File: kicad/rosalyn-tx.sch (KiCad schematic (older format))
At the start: 38 parts, among them J1 USB-C, J2 SWD, J3 TURNIGY 9X, J4 Serial1, J5 Serial2, U1 SPX3819, U2 XC6206, U3 STM32F072C8, U4 E22-EBYTE, U5 SRV05-4

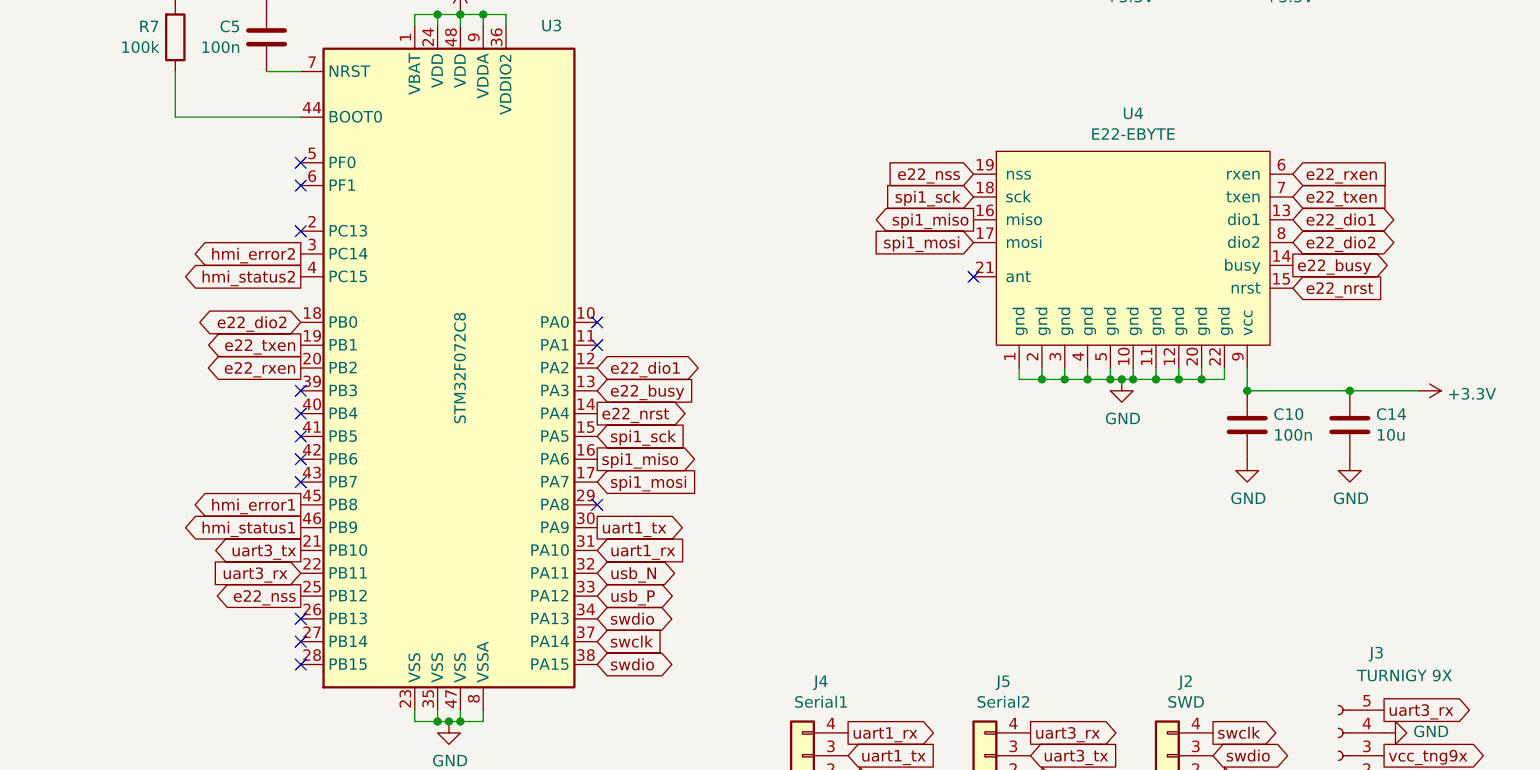
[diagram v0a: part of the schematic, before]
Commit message: added schematic with new radio port names
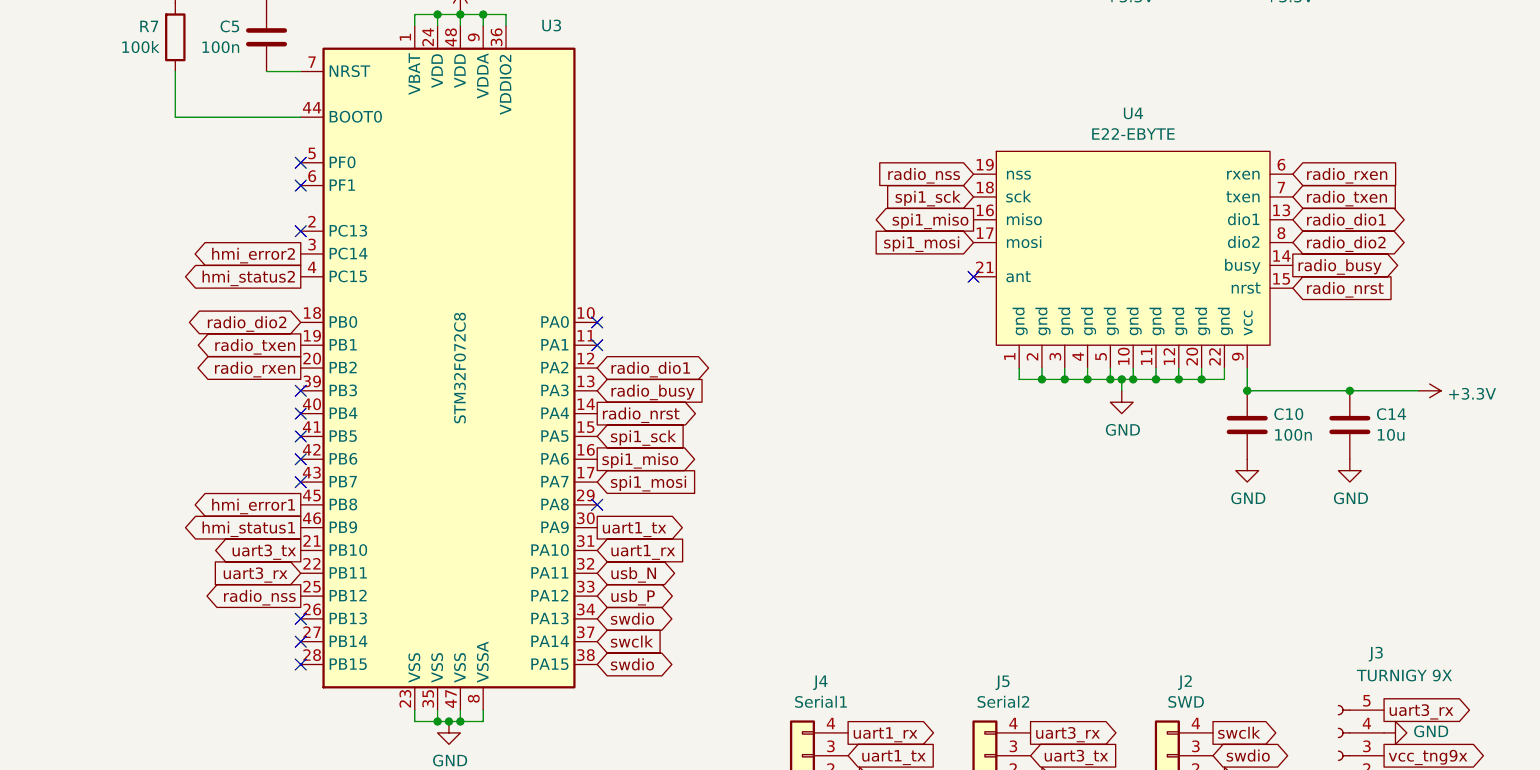
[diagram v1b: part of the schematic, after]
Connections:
- net e22_busy renamed radio_busy
- net e22_dio1 renamed radio_dio1
- net e22_dio2 renamed radio_dio2
- net e22_nrst renamed radio_nrst
- net e22_nss renamed radio_nss
- net e22_rxen renamed radio_rxen
- net e22_txen renamed radio_txen
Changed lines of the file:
@@
 L power:GND #PWR037
 U 1 1 5FC6AB21
-P 9050 3900
+P 9050 3950
 AR Path="/5FC6AB21" Ref="#PWR037"  Part="1"
 AR Path="/5FC29817/5FC6AB21" Ref="#PWR?"  Part="1"
-F 0 "#PWR037" H 9050 3650 50  0001 C CNN
-F 1 "GND" H 9055 3727 50  0000 C CNN
-F 2 "" H 9050 3900 50  0001 C CNN
-F 3 "" H 9050 3900 50  0001 C CNN
-	1    9050 3900
+F 0 "#PWR037" H 9050 3700 50  0001 C CNN
+F 1 "GND" H 9055 3777 50  0000 C CNN
+F 2 "" H 9050 3950 50  0001 C CNN
+F 3 "" H 9050 3950 50  0001 C CNN
+	1    9050 3950
 	1    0    0    -1
 $EndComp
@@
 $EndComp
 Text GLabel 9800 3000 2    50   Input ~ 0
-e22_rxen
+radio_rxen
 Text GLabel 9800 3100 2    50   Input ~ 0
-e22_txen
+radio_txen
 Text GLabel 9800 3200 2    50   BiDi ~ 0
-e22_dio1
+radio_dio1
 Text GLabel 9800 3300 2    50   BiDi ~ 0
-e22_dio2
+radio_dio2
 Text GLabel 9800 3400 2    50   Output ~ 0
-e22_busy
+radio_busy
 Text GLabel 9800 3500 2    50   Input ~ 0
-e22_nrst
+radio_nrst
 Text GLabel 8400 3000 0    50   Input ~ 0
-e22_nss
+radio_nss
 Text GLabel 8400 3100 0    50   Input ~ 0
 spi1_sck
@@
 usb_N
 Text GLabel 5450 3850 0    50   Output ~ 0
-e22_rxen
+radio_rxen
 Text GLabel 5450 3750 0    50   Output ~ 0
-e22_txen
+radio_txen
 Text GLabel 6750 3850 2    50   BiDi ~ 0
-e22_dio1
+radio_dio1
 Text GLabel 5450 3650 0    50   BiDi ~ 0
-e22_dio2
+radio_dio2
 Text GLabel 6750 3950 2    50   Input ~ 0
-e22_busy
+radio_busy
 Text GLabel 6750 4050 2    50   Output ~ 0
-e22_nrst
+radio_nrst
 Text GLabel 5450 4850 0    50   Output ~ 0
-e22_nss
+radio_nss
 Text GLabel 6750 4150 2    50   Input ~ 0
 spi1_sck
@@
 	0    -1   -1   0
 $EndComp
+Wire Wire Line
+	9050 3950 9050 3900
 $EndSCHEMATC

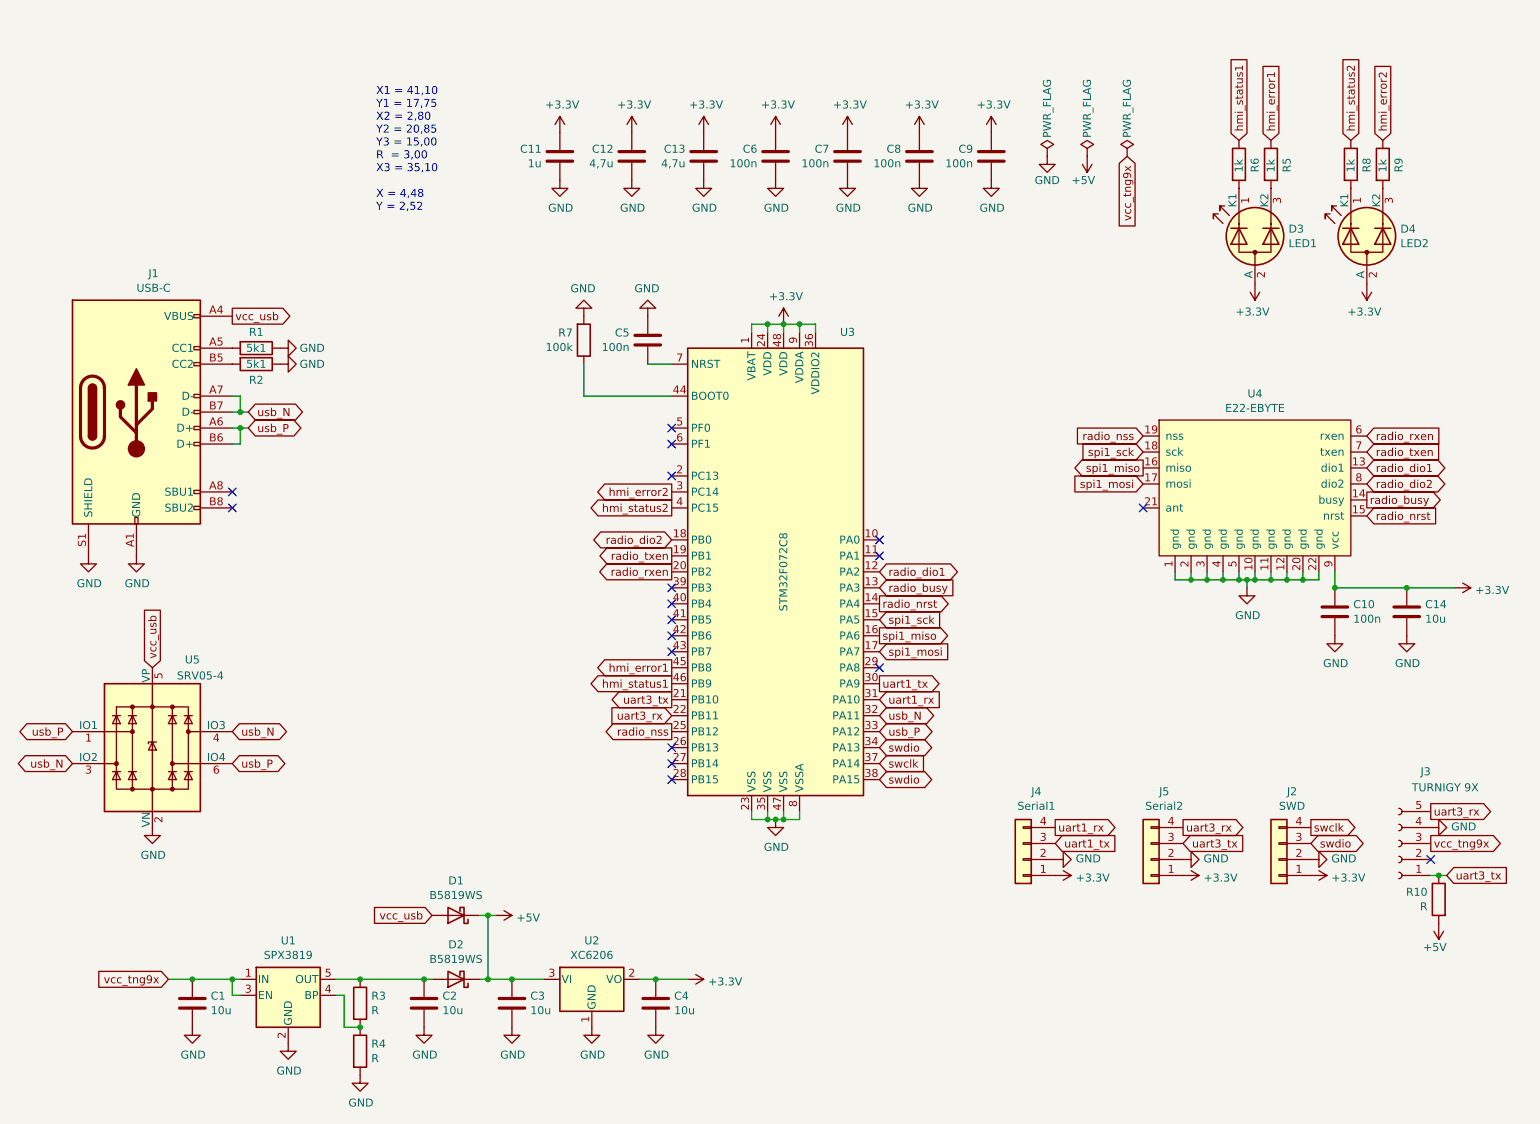
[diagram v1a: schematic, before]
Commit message: added led drivers
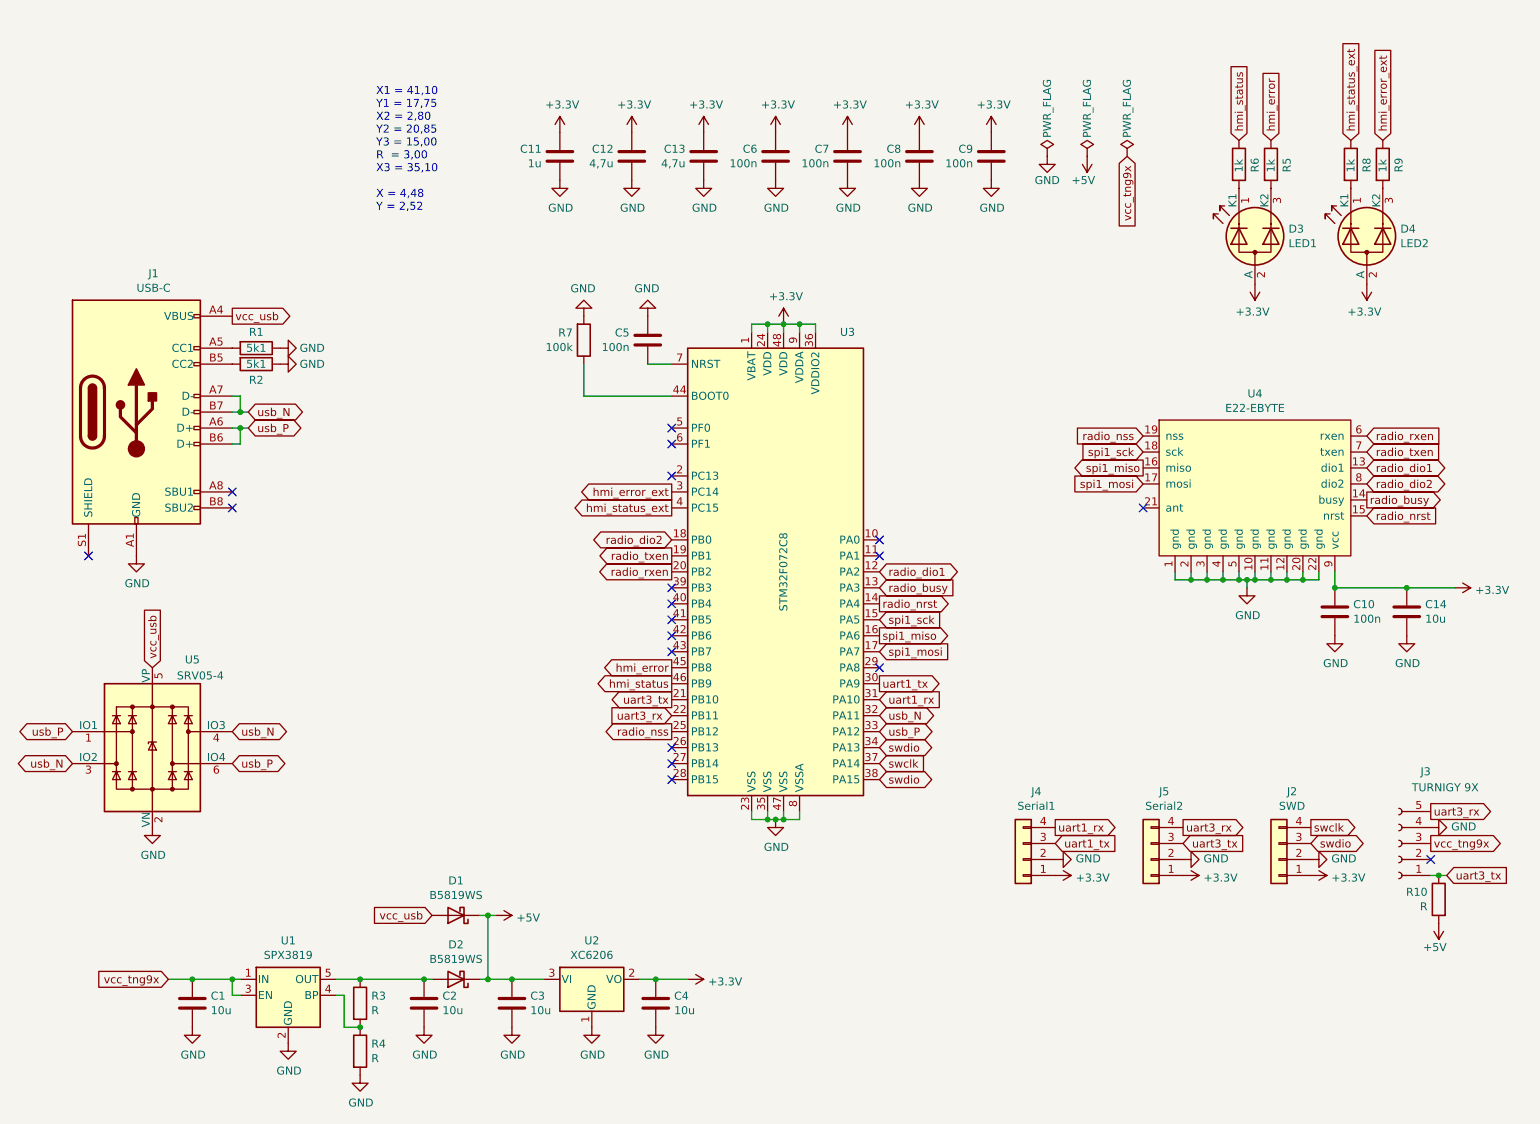
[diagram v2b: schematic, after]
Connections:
- net GND: no longer J1.S1 (SHIELD)
- net hmi_error1 renamed hmi_error
- net hmi_error2 renamed hmi_error_ext
- net hmi_status1 renamed hmi_status
- net hmi_status2 renamed hmi_status_ext
- no-connect marks 18 -> 19
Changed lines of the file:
@@
 vcc_usb
-$Comp
-L power:GND #PWR01
-U 1 1 5FC6AB13
-P 1800 3750
-AR Path="/5FC6AB13" Ref="#PWR01"  Part="1"
-AR Path="/5FC29817/5FC6AB13" Ref="#PWR?"  Part="1"
-F 0 "#PWR01" H 1800 3500 50  0001 C CNN
-F 1 "GND" H 1805 3577 50  0000 C CNN
-F 2 "" H 1800 3750 50  0001 C CNN
-F 3 "" H 1800 3750 50  0001 C CNN
-	1    1800 3750
-	1    0    0    -1
-$EndComp
 $Comp
 L power:GND #PWR02
@@
 NoConn ~ 5450 3250
 Text GLabel 5450 3350 0    50   Output ~ 0
-hmi_error2
+hmi_error_ext
 Text GLabel 5450 3450 0    50   Output ~ 0
-hmi_status2
+hmi_status_ext
 $Comp
 L power:+3.3V #PWR012
@@
 $EndComp
 Text GLabel 9000 1150 1    50   Input ~ 0
-hmi_status1
+hmi_status
 Text GLabel 9200 1150 1    50   Input ~ 0
-hmi_error1
+hmi_error
 $Comp
 L Device:R R?
@@
 $EndComp
 Text GLabel 9700 1150 1    50   Input ~ 0
-hmi_status2
+hmi_status_ext
 Text GLabel 9900 1150 1    50   Input ~ 0
-hmi_error2
+hmi_error_ext
 $Comp
 L Device:R R?
@@
 $EndComp
 Text GLabel 5450 4450 0    50   Output ~ 0
-hmi_error1
+hmi_error
 Text GLabel 5450 4550 0    50   Output ~ 0
-hmi_status1
+hmi_status
 NoConn ~ 5450 2950
 NoConn ~ 5450 3050
@@
 Wire Wire Line
 	9050 3950 9050 3900
+NoConn ~ 1800 3750
 $EndSCHEMATC

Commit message: ppm to transmit is working
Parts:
- R10: value R -> 2k2
- R3: value R -> 68k
- R4: value R -> 22k
- R5, R9: value 1k -> 620
- R6, R8: value 1k -> 220
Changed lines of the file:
@@
 AR Path="/5FC6AC4D" Ref="R6"  Part="1"
 F 0 "R6" V 9100 1250 50  0000 L CNN
-F 1 "1k" V 9000 1250 50  0000 L CNN
+F 1 "220" V 9000 1250 50  0000 L CNN
 F 2 "Resistor_SMD:R_0603_1608Metric" V 8930 1300 50  0001 C CNN
 F 3 "~" H 9000 1300 50  0001 C CNN
@@
 AR Path="/5FC6AC53" Ref="R5"  Part="1"
 F 0 "R5" V 9300 1250 50  0000 L CNN
-F 1 "1k" V 9200 1250 50  0000 L CNN
+F 1 "620" V 9200 1250 50  0000 L CNN
 F 2 "Resistor_SMD:R_0603_1608Metric" V 9130 1300 50  0001 C CNN
 F 3 "~" H 9200 1300 50  0001 C CNN
@@
 AR Path="/5FC6AD30" Ref="R3"  Part="1"
 F 0 "R3" H 3570 6596 50  0000 L CNN
-F 1 "R" H 3570 6505 50  0000 L CNN
+F 1 "68k" H 3570 6505 50  0000 L CNN
 F 2 "Resistor_SMD:R_0603_1608Metric" V 3430 6550 50  0001 C CNN
 F 3 "~" H 3500 6550 50  0001 C CNN
@@
 AR Path="/5FC6AD38" Ref="R4"  Part="1"
 F 0 "R4" H 3570 6896 50  0000 L CNN
-F 1 "R" H 3570 6805 50  0000 L CNN
+F 1 "22k" H 3570 6805 50  0000 L CNN
 F 2 "Resistor_SMD:R_0603_1608Metric" V 3430 6850 50  0001 C CNN
 F 3 "~" H 3500 6850 50  0001 C CNN
@@
 AR Path="/5FA5BF71" Ref="R8"  Part="1"
 F 0 "R8" V 9800 1250 50  0000 L CNN
-F 1 "1k" V 9700 1250 50  0000 L CNN
+F 1 "220" V 9700 1250 50  0000 L CNN
 F 2 "Resistor_SMD:R_0603_1608Metric" V 9630 1300 50  0001 C CNN
 F 3 "~" H 9700 1300 50  0001 C CNN
@@
 AR Path="/5FA5BF77" Ref="R9"  Part="1"
 F 0 "R9" V 10000 1250 50  0000 L CNN
-F 1 "1k" V 9900 1250 50  0000 L CNN
+F 1 "620" V 9900 1250 50  0000 L CNN
 F 2 "Resistor_SMD:R_0603_1608Metric" V 9830 1300 50  0001 C CNN
 F 3 "~" H 9900 1300 50  0001 C CNN
@@
 AR Path="/5FA5908E" Ref="R10"  Part="1"
 F 0 "R10" H 10320 5946 50  0000 L CNN
-F 1 "R" H 10320 5855 50  0000 L CNN
+F 1 "2k2" H 10320 5855 50  0000 L CNN
 F 2 "Resistor_SMD:R_0603_1608Metric" V 10180 5900 50  0001 C CNN
 F 3 "~" H 10250 5900 50  0001 C CNN
